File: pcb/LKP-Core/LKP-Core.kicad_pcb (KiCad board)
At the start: 2 copper layers, 41 x 35 mm, 34 parts, among them J1 Intercon L, J2 Intercon R, J3 Power JST PH, J4 IO, J5 SWD, J6 WS281x, U1 CY8C4246AZI-M445

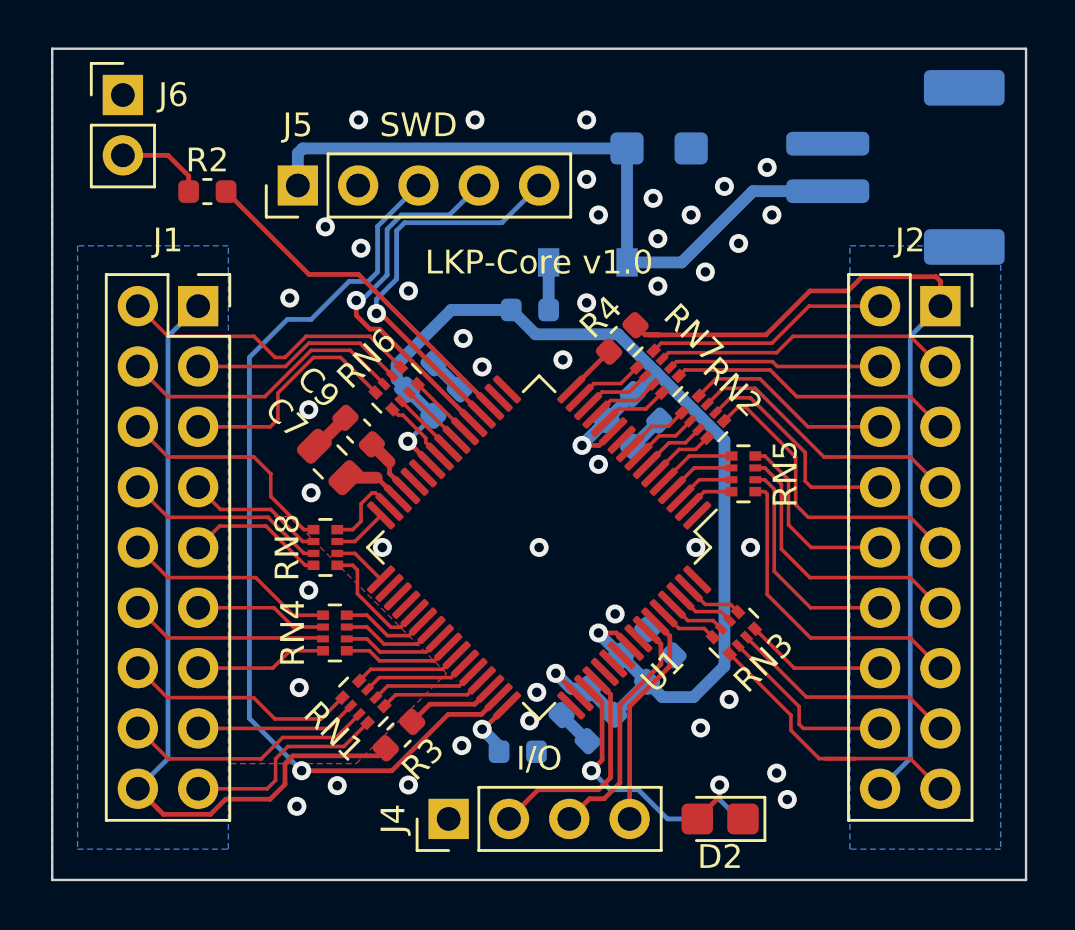
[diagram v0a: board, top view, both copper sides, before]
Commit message: As long as I did it long time ago
Update with parts I have and I want to use to 1.2b, maybe will use it later
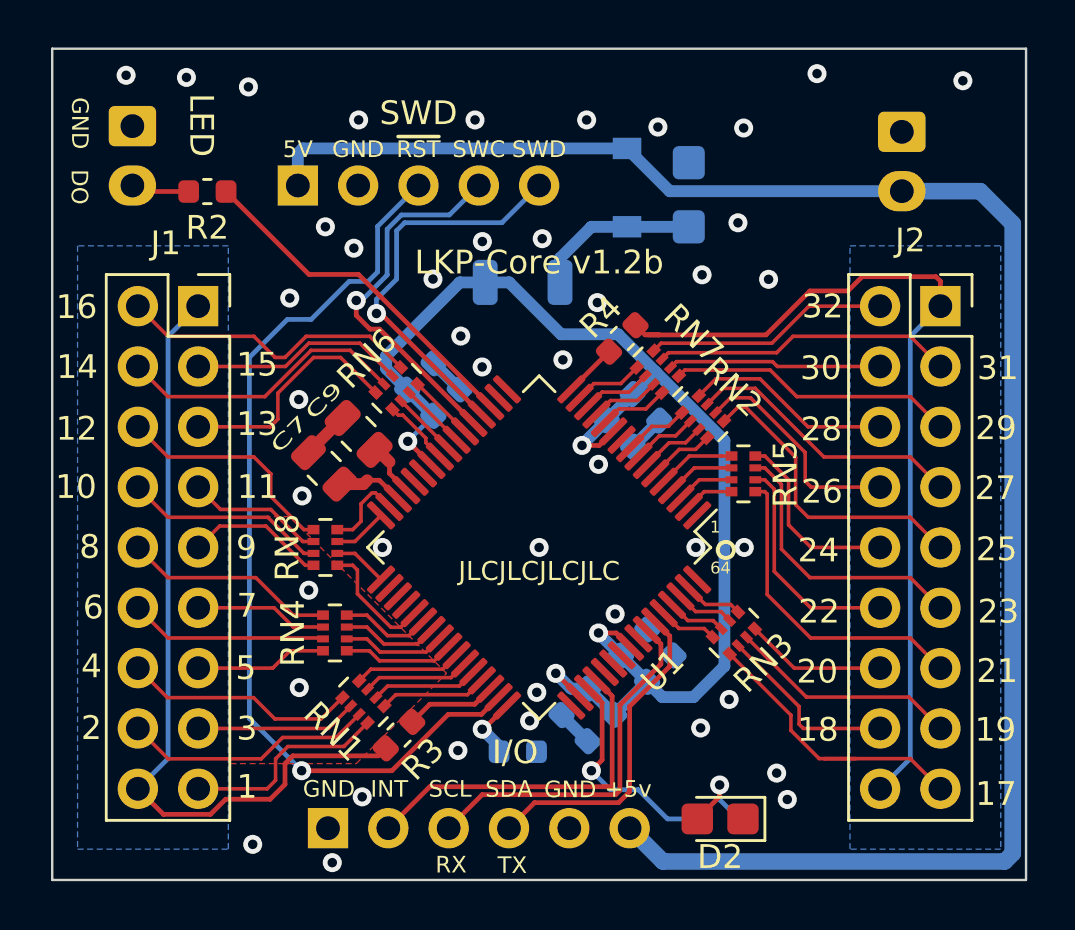
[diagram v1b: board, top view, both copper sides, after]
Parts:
- C9: footprint Capacitor_SMD:C_0603_1608Metric -> Capacitor_SMD:C_0805_2012Metric
- FB1: footprint Inductor_SMD:L_0603_1608Metric -> Inductor_SMD:L_1206_3216Metric
- J3: value Power JST PH -> Power JST XH; footprint Connector_JST:JST_PH_S2B-PH-SM4-TB_1x02-1MP_P2.00mm_Horizontal -> Connector_JST:JST_XH_B2B-XH-A_1x02_P2.50mm_Vertical
- J4: footprint Connector_PinHeader_2.54mm:PinHeader_1x04_P2.54mm_Vertical -> Connector_PinHeader_2.54mm:PinHeader_1x06_P2.54mm_Vertical; moved to B.Cu
- J5: moved to B.Cu
- J6: footprint Connector_PinHeader_2.54mm:PinHeader_1x02_P2.54mm_Vertical -> Connector_JST:JST_XH_B2B-XH-A_1x02_P2.50mm_Vertical; moved to B.Cu
- moved J4 5.09 mm to (138.0, 109.8), turned to -90 degrees
- moved D1 3.56 mm to (150.6, 82.8), turned to 90 degrees
- moved C12 2.32 mm to (153.2, 83.2), turned to 90 degrees
- moved J3 1.52 mm to (162.1, 80.5)
- moved J6 1.37 mm to (129.8, 80.3), turned to -90 degrees
- moved FB1 1.20 mm to (146.2, 86.8)
- moved C7 0.37 mm to (137.8, 94.7)
- moved C9 0.12 mm to (139.3, 93.2)
- turned J5 to -90 degrees
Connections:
- C12 pad 1: +5V -> Net-(C12-Pad1)
- D1 pad 1: Net-(D1-Pad1) -> Net-(C12-Pad1)
- FB1 pad 2: Net-(D1-Pad1) -> Net-(C12-Pad1)
- U1 pad 1: Net-(U1-Pad1) -> unconnected-(U1-Pad1)
- U1 pad 18: Net-(U1-Pad18) -> unconnected-(U1-Pad18)
- U1 pad 27: Net-(U1-Pad27) -> unconnected-(U1-Pad27)
- U1 pad 28: Net-(U1-Pad28) -> unconnected-(U1-Pad28)
- U1 pad 53: Net-(U1-Pad53) -> unconnected-(U1-Pad53)
- U1 pad 54: Net-(U1-Pad54) -> unconnected-(U1-Pad54)
- U1 pad 55: Net-(U1-Pad55) -> unconnected-(U1-Pad55)
- U1 pad 64: Net-(U1-Pad64) -> unconnected-(U1-Pad64)
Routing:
- net +5V: track 29.8 -> 76.2 mm
- net Net-(C12-Pad1): track 0.00 -> 6.99 mm
- net /I2C_SCL: track 10.2 -> 15.8 mm
- net /INT: track 9.34 -> 14.9 mm
- net /I2C_SDA: track 9.26 -> 13.8 mm
- net Net-(D1-Pad1): track 2.00 -> 0.00 mm
- net VDD: track 53.3 -> 55.1 mm
- net /LED: track 3.78 -> 2.47 mm
- net GND: track 6.79 -> 6.72 mm, vias 42 -> 43
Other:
- net class CapSense removed
- net class Default removed
- net class Power removed
- rule pad_to_mask_clearance: 0.05 -> 0
- board text added: "+"
- board text added: "+5v"
- board text added: "1"
- board text added: "10"
- board text added: "11"
- board text added: "12"
- board text added: "13"
- board text added: "14"
- board text added: "15"
- board text added: "16"
- board text added: "17"
- board text added: "18"
- board text added: "19"
- board text added: "2"
- board text added: "20"
- board text added: "21"
- board text added: "22"
- board text added: "23"
- board text added: "24"
- board text added: "25"
- board text added: "26"
- board text added: "27"
- board text added: "28"
- board text added: "29"
- board text added: "3"
- board text added: "30"
- board text added: "31"
- board text added: "32"
- board text added: "4"
- board text added: "5"
- board text added: "5V"
- board text added: "6"
- board text added: "64"
- board text added: "7"
- board text added: "8"
- board text added: "9"
- board text added: "DO"
- board text added: "Fab batch identifier. Only used for JLCPCB. Disable before exporting for other fabs."
- board text added: "GND"
- board text added: "INT"
- board text added: "JLCJLCJLCJLC"
- board text added: "LED"
- board text added: "LKP-Core v1.2b"
- board text added: "RX"
- board text added: "SCL"
- board text added: "SDA"
- board text added: "SWC"
- board text added: "TX"
- board text added: "~{RST}"
- board text added: "°"
- board text removed: "LKP-Core v1.0"
